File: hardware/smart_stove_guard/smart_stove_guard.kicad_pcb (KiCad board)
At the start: 2 copper layers, 70.1 x 50.9 mm, 34 parts, among them IC1 BS412, J1 12401948E412A, J2 AX-1203D-LF, J3 IO Expansion, U1 ESP32-C6-WROOM-1-N4, U2 MLX90614ESF-AAA-000-TU, U3 AMS1117-3.3

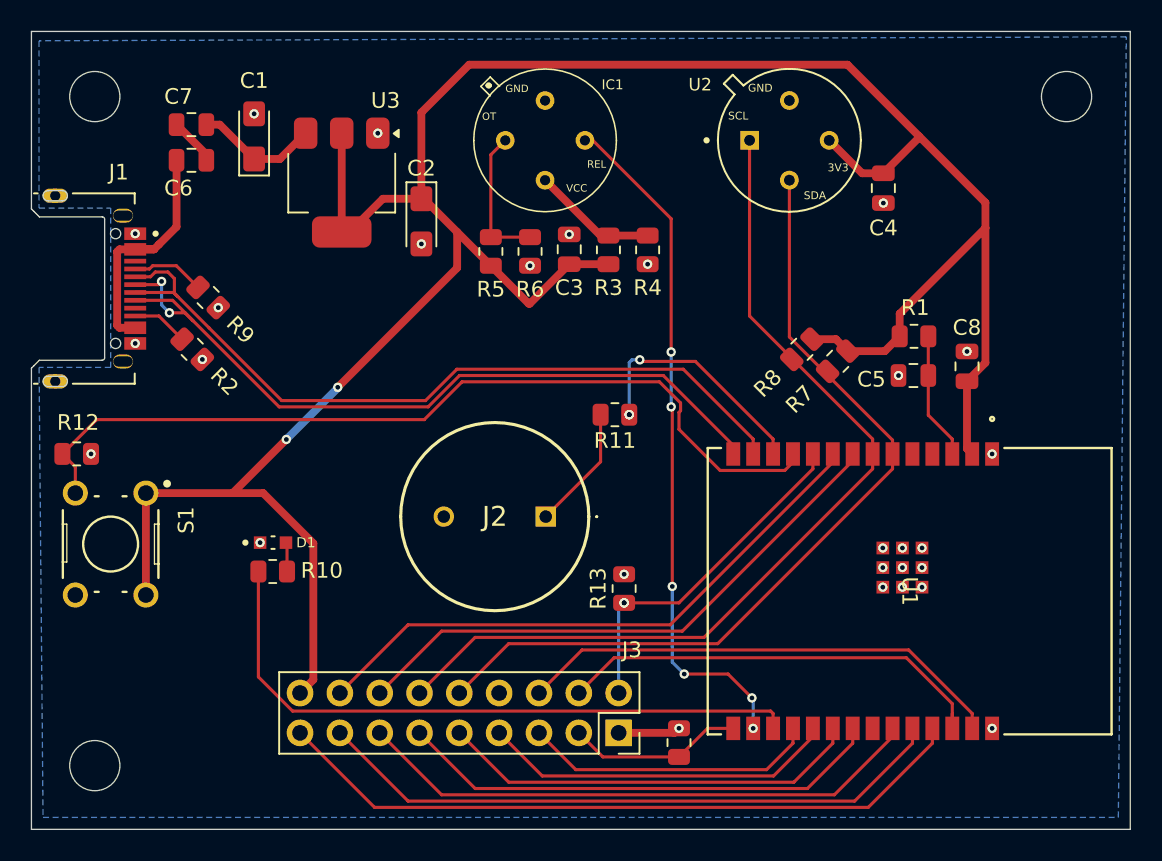
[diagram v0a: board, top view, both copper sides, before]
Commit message: Finished layout, but going to skip for time and budget
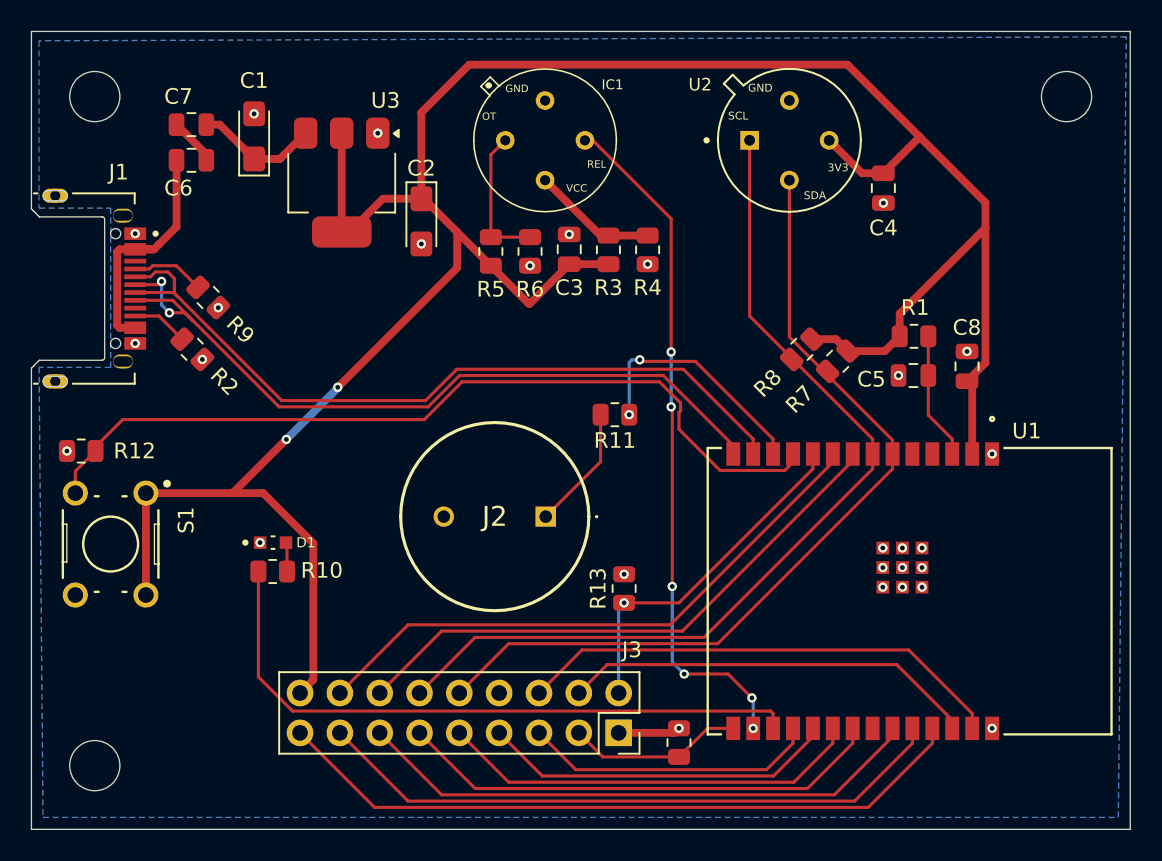
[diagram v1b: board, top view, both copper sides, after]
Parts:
- moved R12 0.34 mm to (81.2, 111.8), turned to 180 degrees
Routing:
- net IO3: track 28.5 -> 26.6 mm
- net USER_BUTTON: track 55.6 -> 53.9 mm
- net BUZZER: vias 3 -> 2
- net BOOT_1: vias 2 -> 1
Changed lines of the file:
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@@
 			(outputformat 1)
 			(mirror no)
-			(drillshape 1)
+			(drillshape 0)
 			(scaleselection 1)
-			(outputdirectory "")
+			(outputdirectory "gerber1/")
 		)
 	)
@@
 	(footprint "Resistor_SMD:R_0805_2012Metric"
 		(layer "F.Cu")
-		(at 80.8875 111.9443)
+		(at 81.1765 111.76 180)
 		(descr "Resistor SMD 0805 (2012 Metric), square (rectangular) end terminal, IPC-7351 nominal, (Body size source: IPC-SM-782 page 72, https://www.pcb-3d.com/wordpress/wp-content/uploads/ipc-sm-782a_amendment_1_and_2.pdf), generated with kicad-footprint-generator")
 		(tags "resistor")
 		(property "Reference" "R12"
-			(at 0.0875 -2 0)
+			(at -3.4055 0 0)
 			(layer "F.SilkS")
 			(effects
@@
 		(attr smd)
 		(fp_line
-			(start -0.227064 -0.735)
-			(end 0.227064 -0.735)
+			(start -0.227064 0.735)
+			(end 0.227064 0.735)
 			(stroke
 				(width 0.12)
@@
 		)
 		(fp_line
-			(start -0.227064 0.735)
-			(end 0.227064 0.735)
+			(start -0.227064 -0.735)
+			(end 0.227064 -0.735)
 			(stroke
 				(width 0.12)
@@
 		)
 		(fp_line
-			(start -1.68 -0.95)
-			(end 1.68 -0.95)
+			(start 1.68 0.95)
+			(end -1.68 0.95)
 			(stroke
 				(width 0.05)
@@
 		)
 		(fp_line
-			(start -1.68 0.95)
-			(end -1.68 -0.95)
+			(start 1.68 -0.95)
+			(end 1.68 0.95)
 			(stroke
 				(width 0.05)
@@
 		)
 		(fp_line
-			(start 1.68 -0.95)
-			(end 1.68 0.95)
+			(start -1.68 0.95)
+			(end -1.68 -0.95)
 			(stroke
 				(width 0.05)
@@
 		)
 		(fp_line
-			(start 1.68 0.95)
-			(end -1.68 0.95)
+			(start -1.68 -0.95)
+			(end 1.68 -0.95)
 			(stroke
 				(width 0.05)
@@
 		)
 		(fp_line
-			(start -1 -0.625)
-			(end 1 -0.625)
+			(start 1 0.625)
+			(end -1 0.625)
 			(stroke
 				(width 0.1)
@@
 		)
 		(fp_line
-			(start -1 0.625)
-			(end -1 -0.625)
+			(start 1 -0.625)
+			(end 1 0.625)
 			(stroke
 				(width 0.1)
@@
 		)
 		(fp_line
-			(start 1 -0.625)
-			(end 1 0.625)
+			(start -1 0.625)
+			(end -1 -0.625)
 			(stroke
 				(width 0.1)
@@
 		)
 		(fp_line
-			(start 1 0.625)
-			(end -1 0.625)
+			(start -1 -0.625)
+			(end 1 -0.625)
 			(stroke
 				(width 0.1)
@@
 		)
 		(pad "1" smd roundrect
-			(at -0.9125 0)
+			(at -0.9125 0 180)
 			(size 1.025 1.4)
 			(layers "F.Cu" "F.Mask" "F.Paste")
@@
 		)
 		(pad "2" smd roundrect
-			(at 0.9125 0)
+			(at 0.9125 0 180)
 			(size 1.025 1.4)
 			(layers "F.Cu" "F.Mask" "F.Paste")
@@
 		(tags "ESP32-C6-WROOM-1-N4 ")
 		(property "Reference" "U1"
-			(at 0 0 270)
+			(at -10.2093 -7.468 0)
 			(unlocked yes)
 			(layer "F.SilkS")
@@
 			(layer "F.SilkS")
 		)
-		(fp_poly
-			(pts
-				(xy -9.0043 -12.7508) (xy -9.0043 -6.7564) (xy 9.0043 -6.7564) (xy 9.0043 -12.7508)
-			)
-			(stroke
-				(width 0)
-				(type solid)
-			)
-			(fill yes)
-			(layer "Eco2.User")
-		)
 		(fp_line
 			(start -9.2583 13.0048)
@@
 	)
 	(via
-		(at 81.8 111.9443)
+		(at 117.3 99.8443)
 		(size 0.6)
 		(drill 0.3)
@@
 	)
 	(via
-		(at 117.3 99.8443)
+		(at 102.87 98.552)
 		(size 0.6)
 		(drill 0.3)
@@
 	)
 	(via
-		(at 102.87 98.552)
+		(at 134.8 119.1943)
 		(size 0.6)
 		(drill 0.3)
@@
 	)
 	(via
-		(at 134.8 119.1943)
+		(at 112.3 97.9443)
 		(size 0.6)
 		(drill 0.3)
@@
 	)
 	(via
-		(at 112.3 97.9443)
+		(at 92.202 90.254)
 		(size 0.6)
 		(drill 0.3)
@@
 	)
 	(via
-		(at 92.202 90.254)
+		(at 80.264 111.76)
 		(size 0.6)
 		(drill 0.3)
@@
 	)
 	(segment
-		(start 137.668 111.6173)
-		(end 138 111.9493)
-		(width 0.5)
-		(layer "F.Cu")
-		(net 3)
-	)
-	(segment
 		(start 95.98 117.646)
 		(end 95.98 126.3443)
@@
 	)
 	(segment
+		(start 137.668 107.31)
+		(end 138 107.642)
+		(width 0.5)
+		(layer "F.Cu")
+		(net 3)
+	)
+	(segment
 		(start 112.3 99.8443)
 		(end 114.8 99.8443)
@@
 	)
 	(segment
-		(start 137.668 107.31)
-		(end 137.668 111.6173)
-		(width 0.5)
-		(layer "F.Cu")
-		(net 3)
-	)
-	(segment
 		(start 127.78247 104.62753)
 		(end 129.30647 104.62753)
@@
 	)
 	(segment
+		(start 138 107.642)
+		(end 138 111.9493)
+		(width 0.5)
+		(layer "F.Cu")
+		(net 3)
+	)
+	(segment
 		(start 130.9817 94.046)
 		(end 128.88 91.9443)
@@
 	)
 	(segment
-		(start 136.73 128.5)
-		(end 136.73 129.4493)
+		(start 114.7213 125.383)
+		(end 112.91 127.1943)
 		(width 0.2)
 		(layer "F.Cu")
@@
 	)
 	(segment
-		(start 112.91 127.1943)
-		(end 115.16 124.9443)
+		(start 133.1895 125.383)
+		(end 114.7213 125.383)
 		(width 0.2)
 		(layer "F.Cu")
@@
 	)
 	(segment
-		(start 115.16 124.9443)
-		(end 133.8 124.9443)
+		(start 136.73 128.9235)
+		(end 133.1895 125.383)
 		(width 0.2)
 		(layer "F.Cu")
@@
 	)
 	(segment
-		(start 133.8 124.9443)
-		(end 136.73 127.8743)
-		(width 0.2)
-		(layer "F.Cu")
-		(net 8)
-	)
-	(segment
-		(start 136.73 127.8743)
-		(end 136.73 129.4493)
+		(start 136.73 129.4493)
+		(end 136.73 128.9235)
 		(width 0.2)
 		(layer "F.Cu")
@@
 		(net 13)
 	)
-	(via
-		(at 115.8 121.4443)
-		(size 0.6)
-		(drill 0.3)
-		(layers "F.Cu" "B.Cu")
-		(net 13)
-	)
 	(segment
 		(start 115.45 121.7943)
@@
 	)
 	(via
-		(at 116.125 109.4443)
-		(size 0.6)
-		(drill 0.3)
-		(layers "F.Cu" "B.Cu")
-		(net 29)
-	)
-	(via
 		(at 116.8 105.9433)
 		(size 0.6)
@@
 	)
 	(segment
-		(start 126.0455 112.9996)
-		(end 126.57 112.4751)
+		(start 83.82 109.7578)
+		(end 103.0536 109.7578)
 		(width 0.2)
 		(layer "F.Cu")
@@
 	)
 	(segment
-		(start 119.3 109.294243)
-		(end 119.3 110.3772)
+		(start 126.0455 112.9996)
+		(end 126.57 112.4751)
 		(width 0.2)
 		(layer "F.Cu")
@@
 	)
 	(segment
-		(start 80.8 112.7693)
-		(end 79.975 111.9443)
+		(start 80.8 113.049)
+		(end 82.089 111.76)
 		(width 0.2)
 		(layer "F.Cu")
@@
 	)
 	(segment
-		(start 126.57 112.4751)
-		(end 126.57 111.9493)
+		(start 119.3 109.294243)
+		(end 119.3 110.3772)
 		(width 0.2)
 		(layer "F.Cu")
@@
 	)
 	(segment
-		(start 79.975 111.9443)
-		(end 82.1615 109.7578)
+		(start 126.57 112.4751)
+		(end 126.57 111.9493)
 		(width 0.2)
 		(layer "F.Cu")
@@
 	)
 	(segment
-		(start 105.4661 107.3453)
-		(end 118.050943 107.3453)
+		(start 82.089 111.4888)
+		(end 83.82 109.7578)
 		(width 0.2)
 		(layer "F.Cu")
@@
 	)
 	(segment
-		(start 121.9224 112.9996)
-		(end 126.0455 112.9996)
+		(start 80.8 114.4443)
+		(end 80.8 113.049)
 		(width 0.2)
 		(layer "F.Cu")
@@
 	)
 	(segment
-		(start 118.050943 107.3453)
-		(end 119.401 108.695357)
+		(start 105.4661 107.3453)
+		(end 118.050943 107.3453)
 		(width 0.2)
 		(layer "F.Cu")
@@
 	)
 	(segment
-		(start 82.1615 109.7578)
-		(end 103.0536 109.7578)
+		(start 121.9224 112.9996)
+		(end 126.0455 112.9996)
 		(width 0.2)
 		(layer "F.Cu")
@@
 	)
 	(segment
-		(start 80.8 114.4443)
-		(end 80.8 112.7693)
+		(start 82.089 111.76)
+		(end 82.089 111.4888)
+		(width 0.2)
+		(layer "F.Cu")
+		(net 30)
+	)
+	(segment
+		(start 118.050943 107.3453)
+		(end 119.401 108.695357)
 		(width 0.2)
 		(layer "F.Cu")
